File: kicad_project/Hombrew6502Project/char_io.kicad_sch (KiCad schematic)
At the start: 36 parts, among them J1001 Parallel LCD, J1002 Parallel LCD, J1003 Parallel LCD, J1004 Parallel LCD, J1005 KMDGX-6S-BS, J1006 KMDGX-6S-BS, Q1001 2N7002K, U1001 74ACT139, U1002 74HC04, U1003 74HC595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

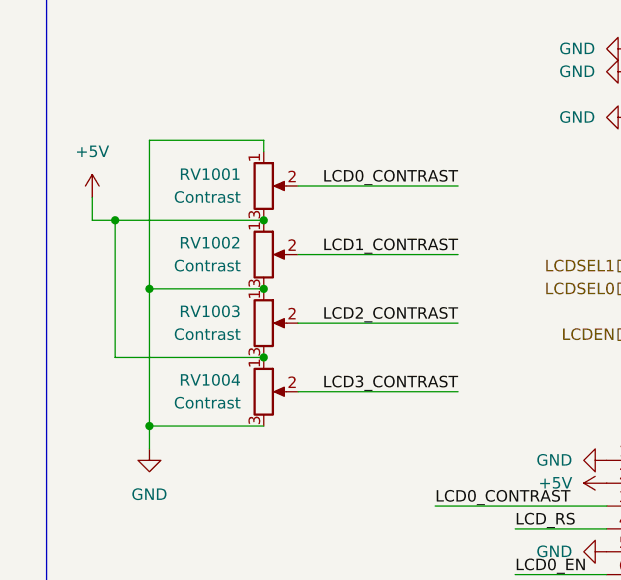
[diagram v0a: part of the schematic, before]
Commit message: footprint assignments and separate project for RAM board
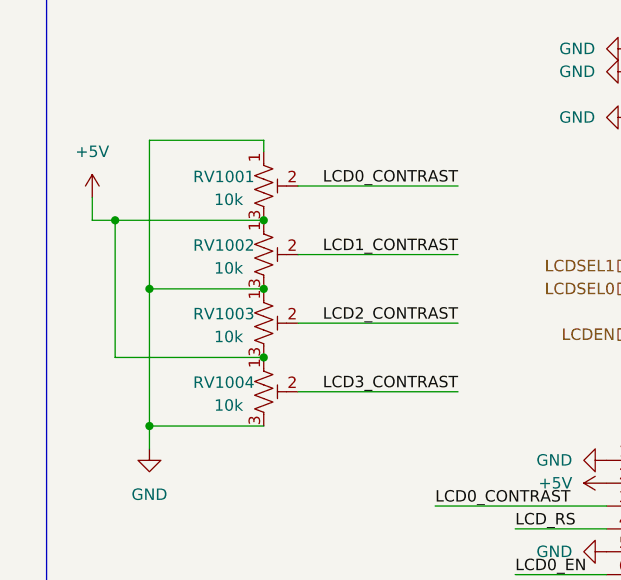
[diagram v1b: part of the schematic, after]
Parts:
- removed RV1001, RV1002, RV1003, RV1004: Contrast, symbol Device:R_Potentiometer
- added RV1001, RV1002, RV1003, RV1004: 10k, Potentiometer_SMD:Potentiometer_Bourns_TC33X_Vertical, symbol Device:R_Potentiometer_Trim_US
- J1001, J1002, J1003, J1004: footprint (none) -> Connector_IDC:IDC-Header_2x08_P2.54mm_Vertical_SMD
- J1006: footprint KMDGX6SBS -> footprints:KMDGX6SBS
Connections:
- net +5V: now also RV1001.3, RV1002.1, RV1003.3, RV1004.1
- net GND: now also RV1001.1, RV1002.3, RV1003.1, RV1004.3
- net LCD0_CONTRAST: now also RV1001.2
- net LCD1_CONTRAST: now also RV1002.2
- net LCD2_CONTRAST: now also RV1003.2
- net LCD3_CONTRAST: now also RV1004.2

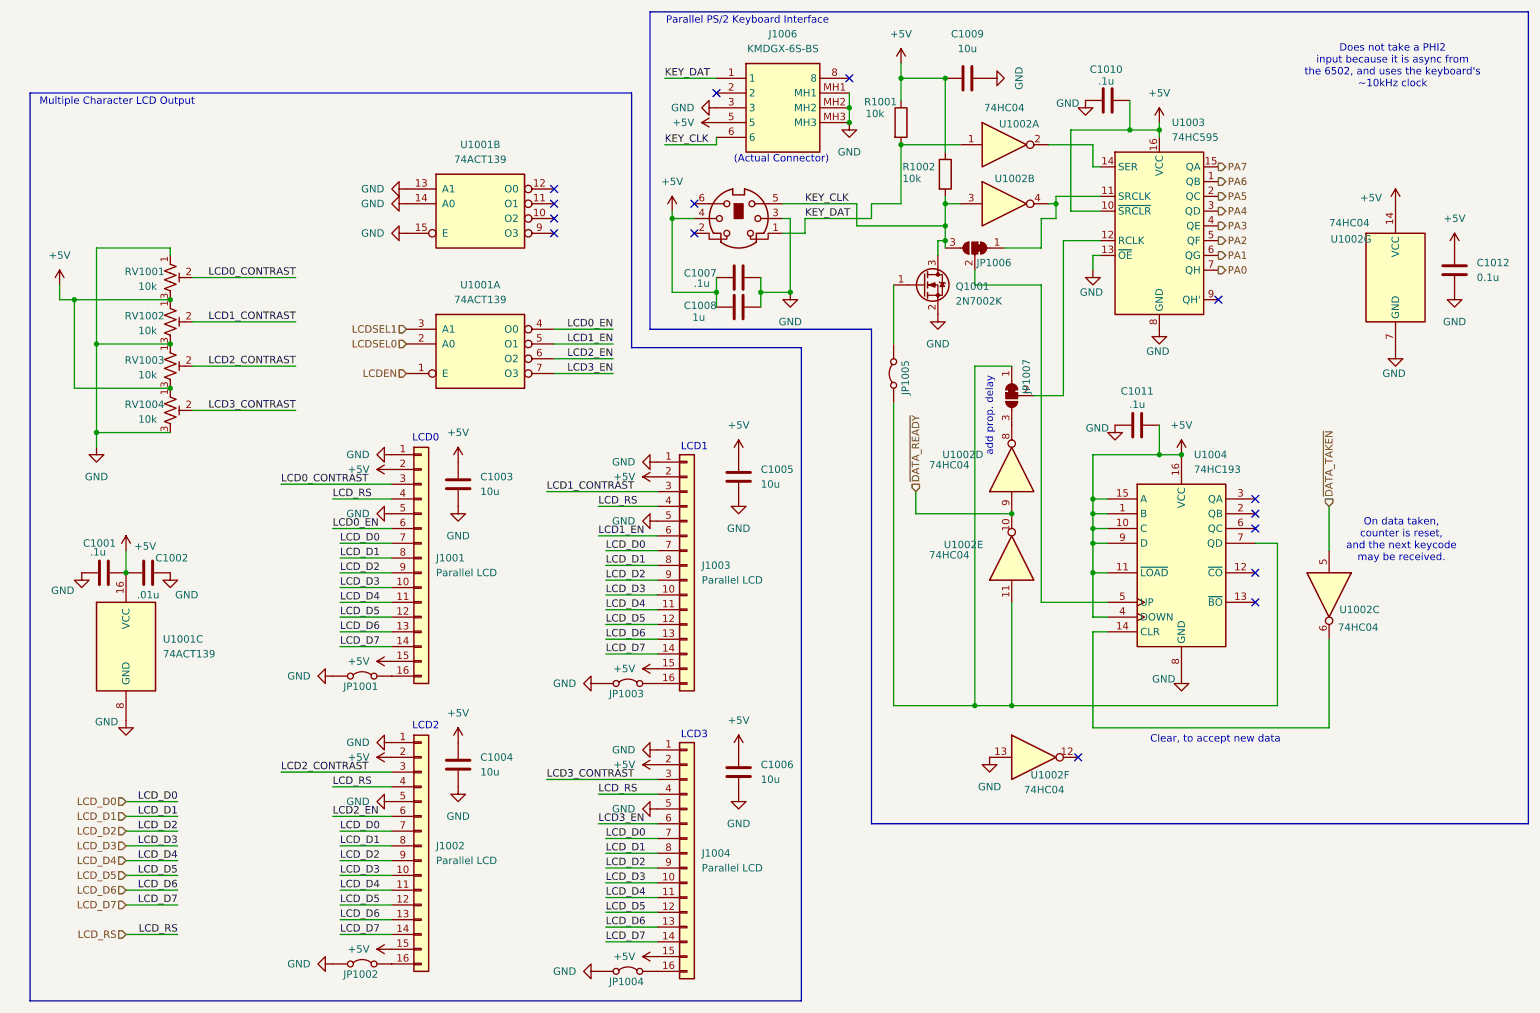
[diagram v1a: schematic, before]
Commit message: Peripheral io layout done; snapshot of current state before redoing much of the rest of the layout.
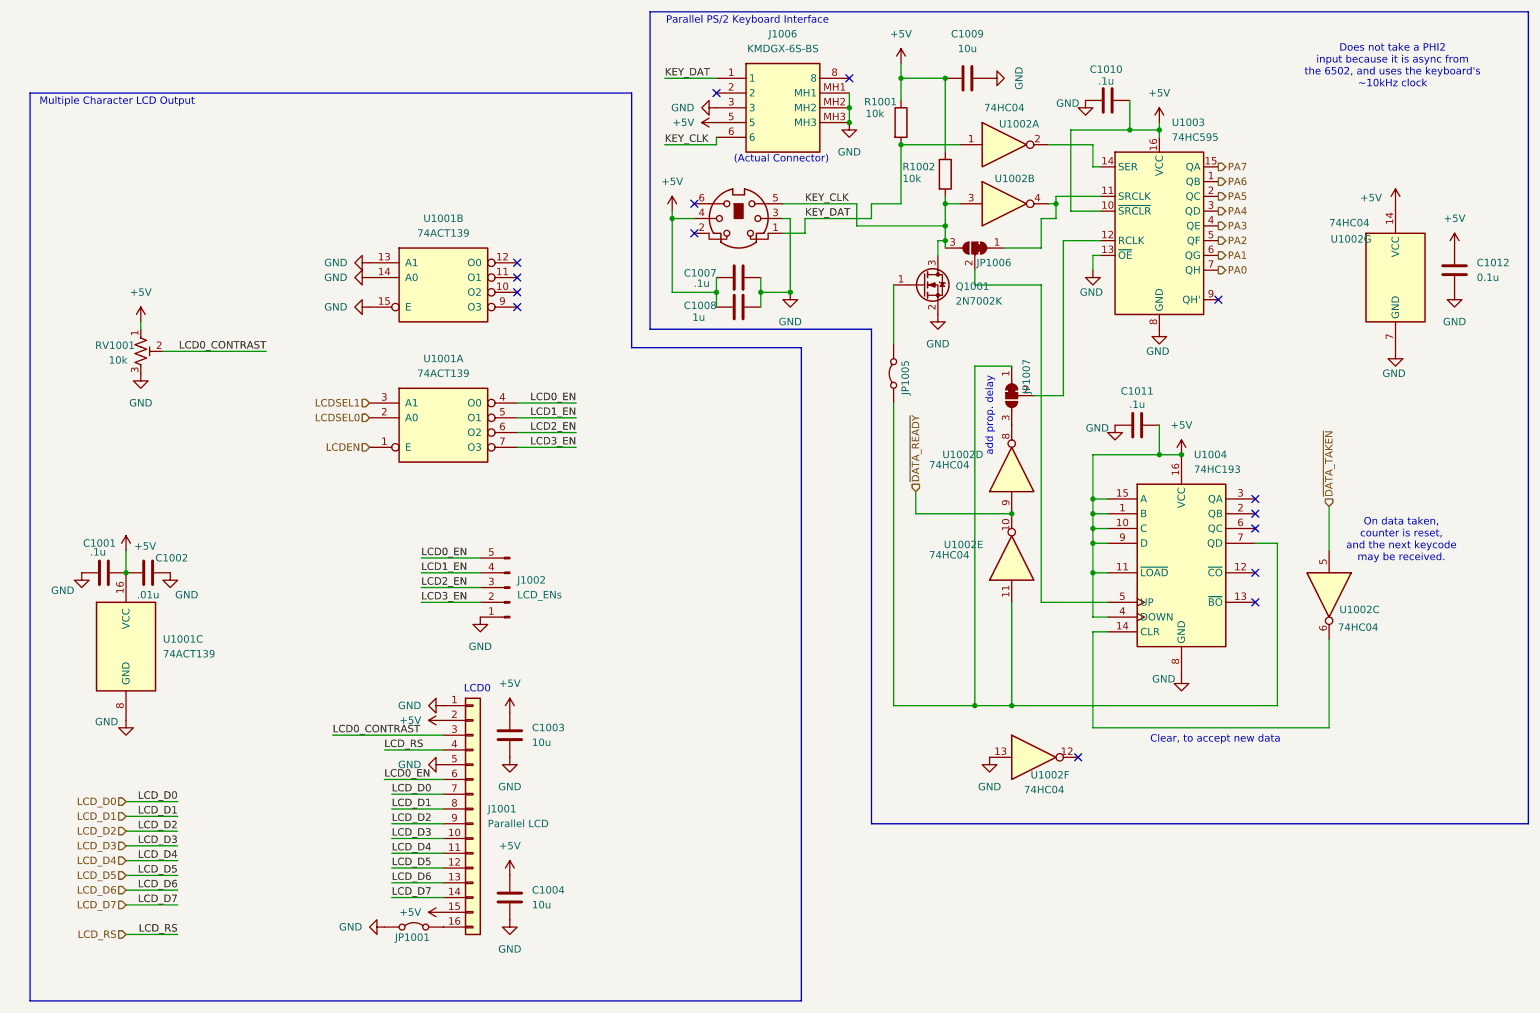
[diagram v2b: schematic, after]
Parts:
- removed C1005, C1006: 10u, Capacitor_SMD:C_0402_1005Metric, symbol Device:C
- removed J1002, J1003, J1004: Parallel LCD, Connector_IDC:IDC-Header_2x08_P2.54mm_Vertical_SMD, symbol Connector_Generic:Conn_01x16
- removed JP1002, JP1003, JP1004: Jumper_2_Bridged, Jumper:SolderJumper-2_P1.3mm_Bridged2Bar_Pad1.0x1.5mm, symbol Jumper:Jumper_2_Bridged
- removed RV1002, RV1003, RV1004: 10k, Potentiometer_SMD:Potentiometer_Bourns_TC33X_Vertical, symbol Device:R_Potentiometer_Trim_US
- added J1002: LCD_ENs, Connector_PinHeader_2.54mm:PinHeader_1x05_P2.54mm_Vertical, symbol Connector:Conn_01x05_Pin
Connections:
- net +5V: now also RV1001.1; no longer RV1001.3
- net GND: now also RV1001.3, J1002.1 (Pin_1); no longer RV1001.1
- net LCD0_EN: now also J1002.5 (Pin_5)
- net LCD1_EN: now also J1002.4 (Pin_4)
- net LCD2_EN: now also J1002.3 (Pin_3)
- net LCD3_EN: now also J1002.2 (Pin_2)
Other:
- note removed: "LCD1"
- note removed: "LCD2"
- note removed: "LCD3"
- moved on the sheet: C1003, C1004, J1001, JP1001, RV1001, U1001A, U1001B
